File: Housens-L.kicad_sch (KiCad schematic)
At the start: 4 parts, among them U1 MCP1603

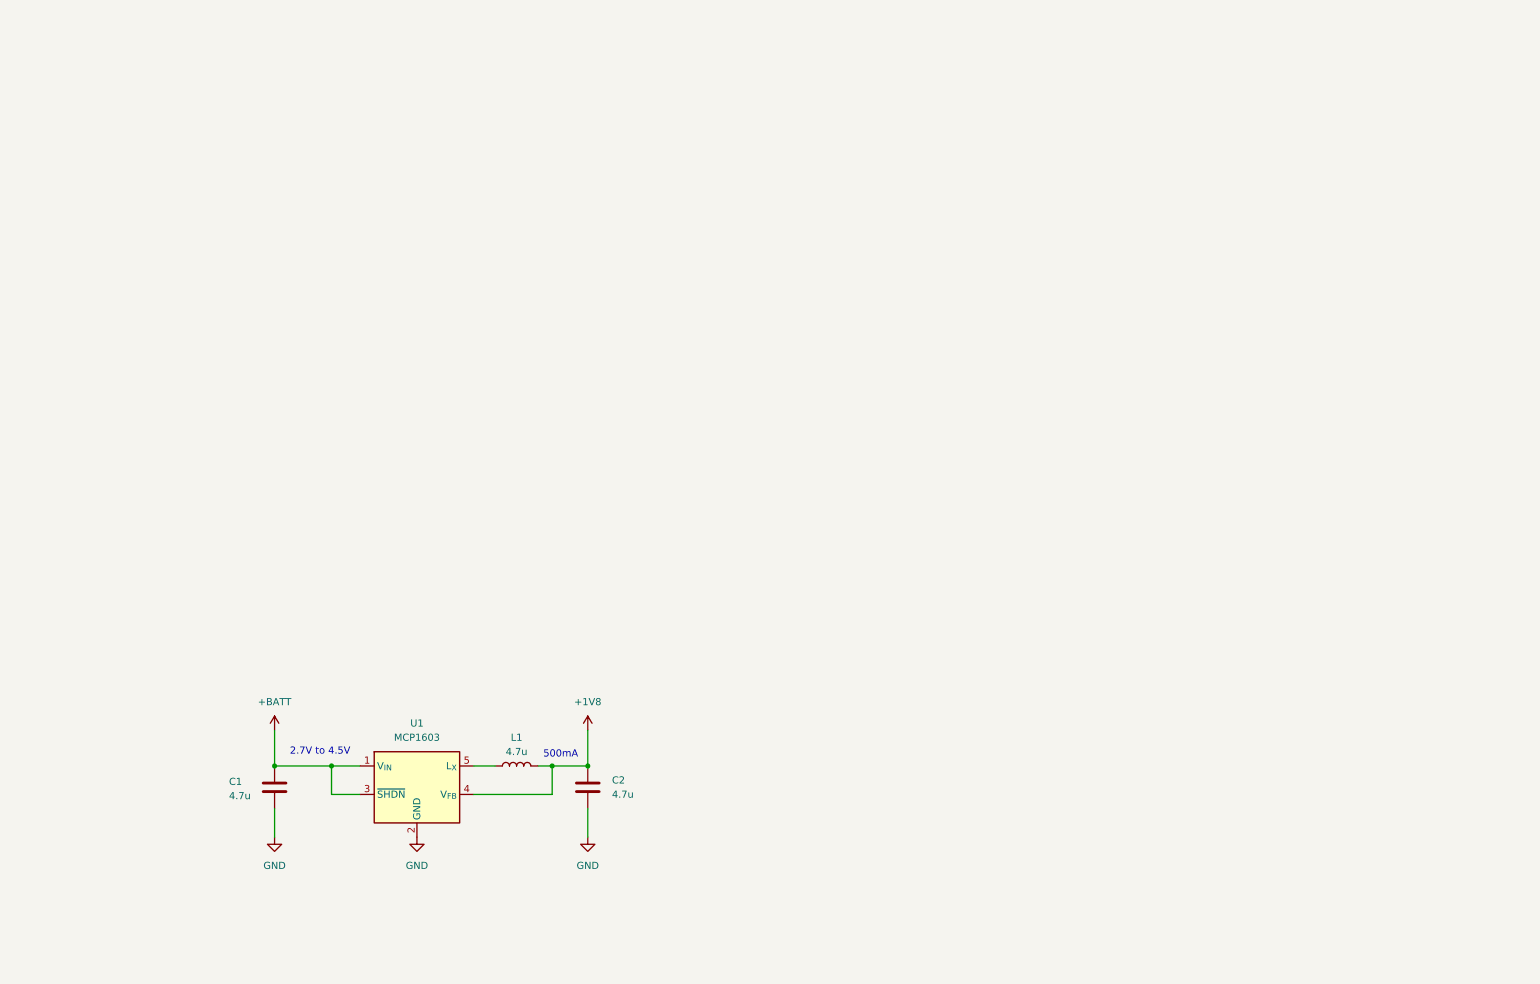
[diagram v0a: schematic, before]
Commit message: Add sensors
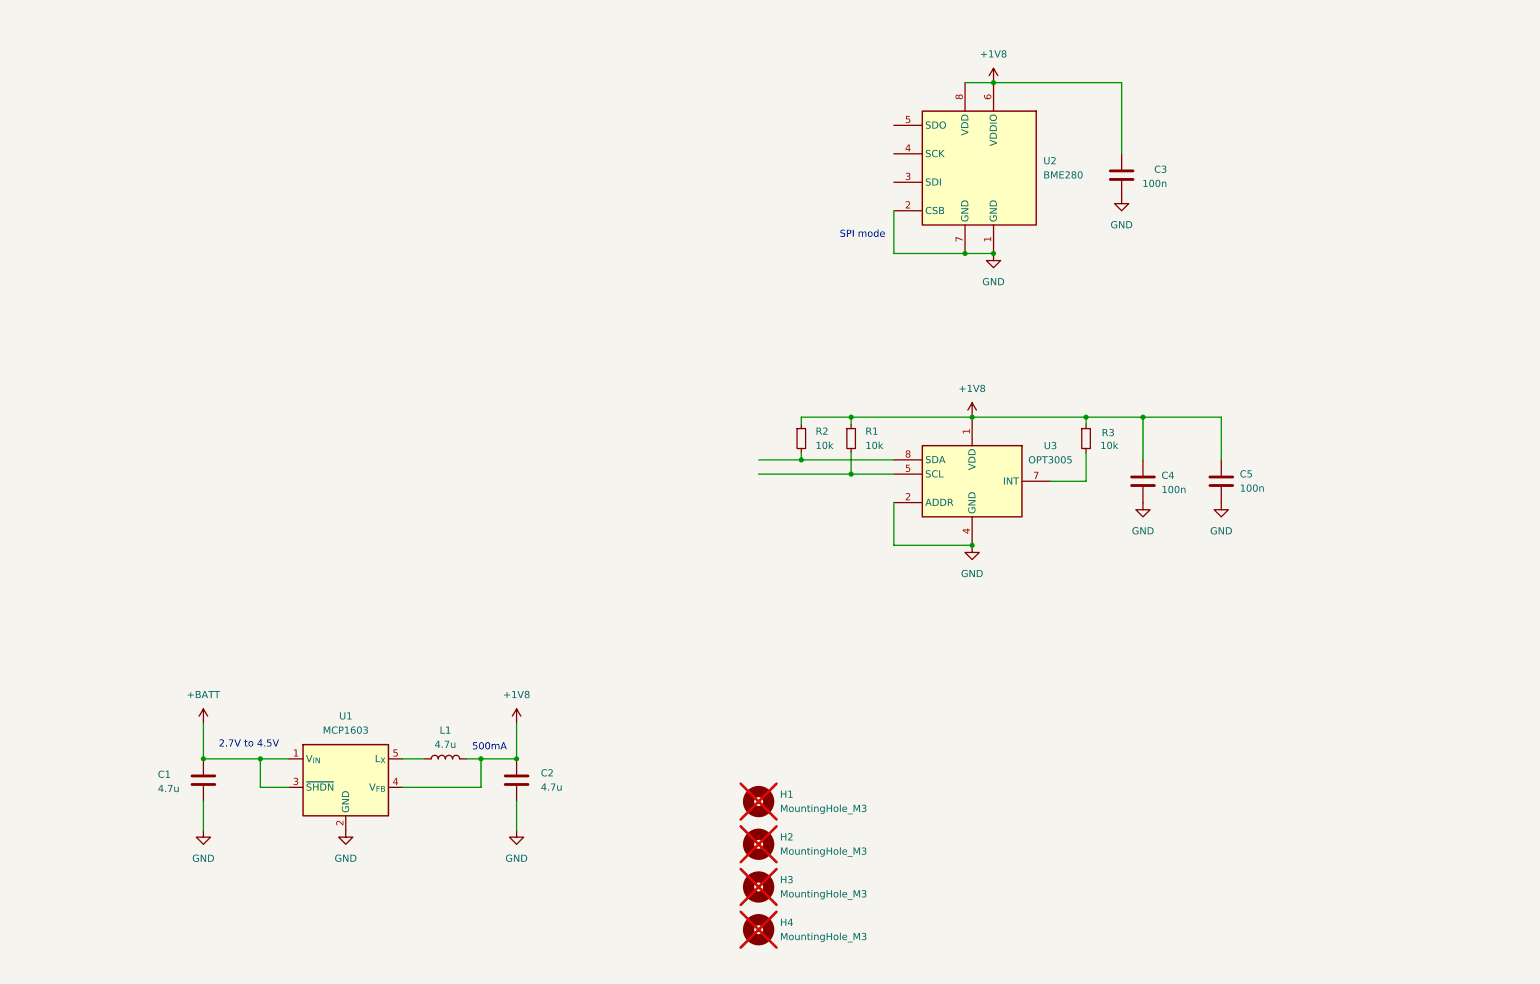
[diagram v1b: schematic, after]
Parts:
- added C3, C4, C5: 100n, Capacitor_SMD:C_0603_1608Metric, symbol Device:C
- added H1, H2, H3, H4: MountingHole_M3, MountingHole:MountingHole_3.2mm_M3, symbol PCM_SL_Mechanical:MountingHole_M3
- added R1, R2, R3: 10k, Resistor_SMD:R_0603_1608Metric, symbol Device:R_Small
- added U2: BME280, Package_LGA:Bosch_LGA-8_2.5x2.5mm_P0.65mm_ClockwisePinNumbering, symbol Sensor:BME280
- added U3: OPT3005, OPT3005DTSR, symbol PCM_OPT3005DTSR:OPT3005DTSR
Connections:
- net +1V8: now also C3.1, C4.1, C5.1, R1.1, R2.1, R3.1, U2.6 (VDDIO), U2.8 (VDD), U3.1 (VDD)
- net GND: now also C3.2, C4.2, C5.2, U2.1 (GND), U2.2 (CSB), U2.7 (GND), U3.2 (ADDR), U3.4 (GND)
- new net: R1.2, U3.5 (SCL)
- new net: R3.2, U3.7 (INT)
- new net: R2.2, U3.8 (SDA)
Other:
- note added: "SPI mode"
- moved on the sheet: C1, C2, L1, U1

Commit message: Add MCU
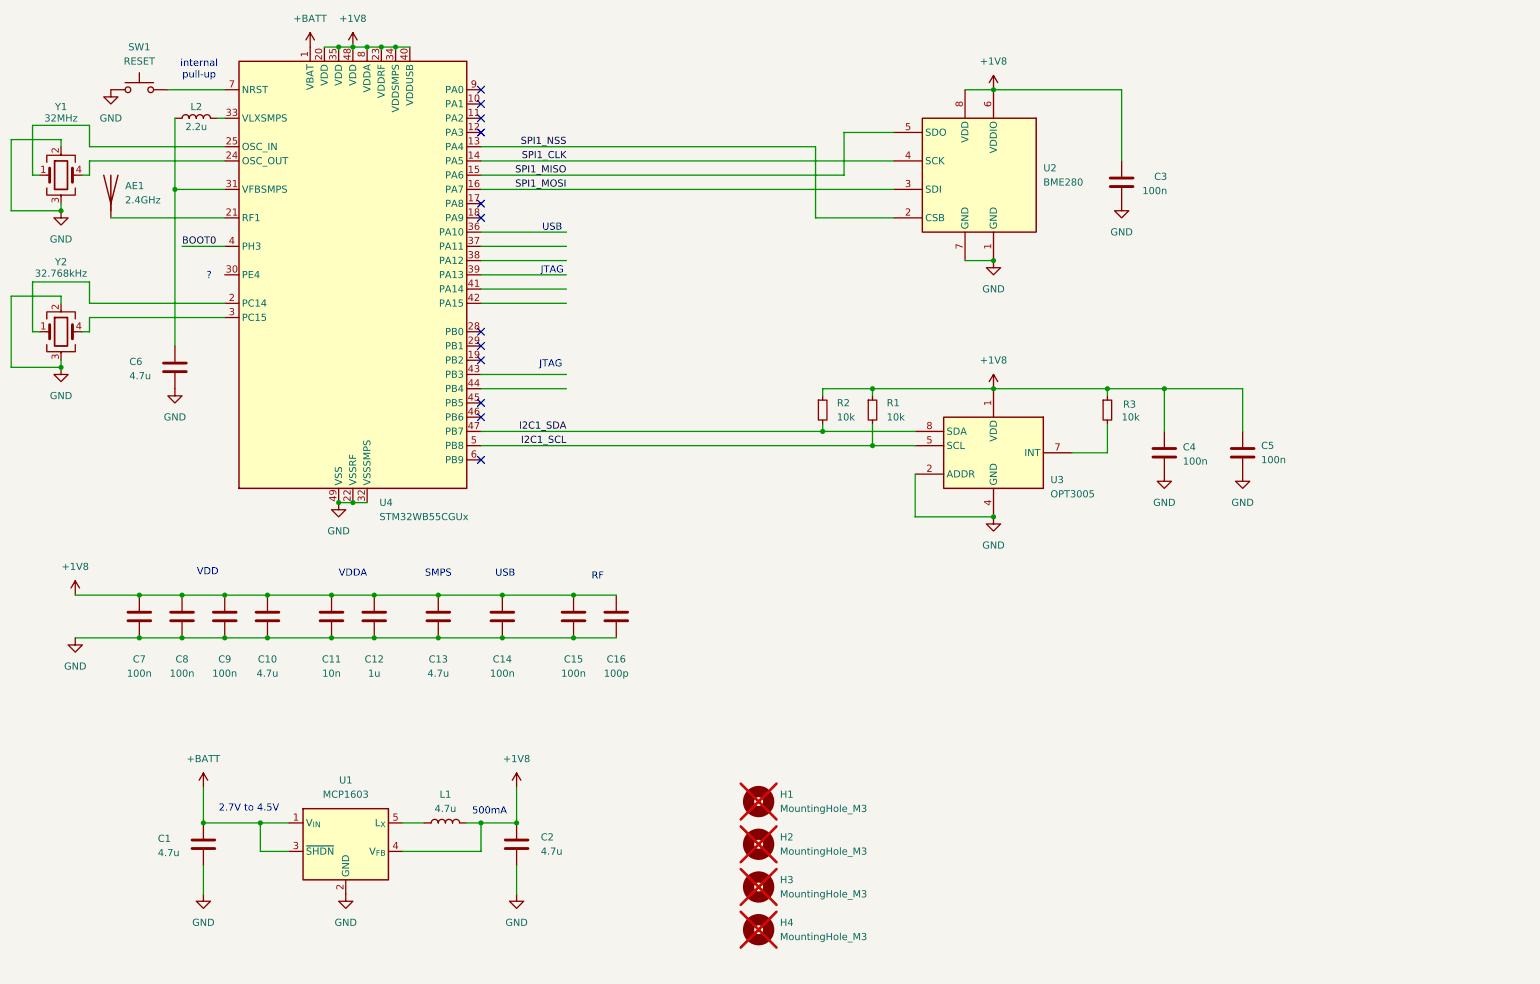
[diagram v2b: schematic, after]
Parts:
- added AE1: 2.4GHz, symbol Device:Antenna
- added C10, C13, C6: 4.7u, Capacitor_SMD:C_0603_1608Metric, symbol Device:C
- added C11: 10n, Capacitor_SMD:C_0603_1608Metric, symbol Device:C
- added C12: 1u, Capacitor_SMD:C_0603_1608Metric, symbol Device:C
- added C14, C15, C7, C8, C9: 100n, Capacitor_SMD:C_0603_1608Metric, symbol Device:C
- added C16: 100p, Capacitor_SMD:C_0603_1608Metric, symbol Device:C
- added L2: 2.2u, Inductor_SMD:L_Wuerth_WE-TPC-3816, symbol Device:L
- added SW1: RESET, Button_Switch_THT:SW_PUSH_6mm, symbol Switch:SW_Push
- added U4: STM32WB55CGUx, Package_DFN_QFN:QFN-48-1EP_7x7mm_P0.5mm_EP5.6x5.6mm, symbol MCU_ST_STM32WB:STM32WB55CGUx
- added Y1: 32MHz, symbol Device:Crystal_GND23
- added Y2: 32.768kHz, symbol Device:Crystal_GND23
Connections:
- net +1V8: now also C10.1, C11.1, C12.1, C13.1, C14.1, C15.1, C16.1, C7.1, C8.1, C9.1, U4.20 (VDD), U4.23 (VDDRF), U4.34 (VDDSMPS), U4.35 (VDD), U4.40 (VDDUSB), U4.48 (VDD), U4.8 (VDDA)
- net +BATT: now also U4.1 (VBAT)
- net GND: now also C10.2, C11.2, C12.2, C13.2, C14.2, C15.2, C16.2, C6.2, C7.2, C8.2, C9.2, SW1.1, U4.22 (VSSRF), U4.32 (VSSSMPS), U4.49 (VSS), Y1.2, Y1.3, Y2.2, Y2.3; no longer U2.2 (CSB)
- net I2C1_SCL: now reaches R1.2, U3.5 (SCL)
- net I2C1_SCL: now also U4.5 (PB8)
- net I2C1_SDA: now reaches R2.2, U3.8 (SDA)
- net I2C1_SDA: now also U4.47 (PB7)
- net SPI1_MOSI: now reaches U2.3 (SDI)
- net SPI1_MOSI: now also U4.16 (PA7)
- net SPI1_CLK: now reaches U2.4 (SCK)
- net SPI1_CLK: now also U4.14 (PA5)
- net SPI1_MISO: now reaches U2.5 (SDO)
- net SPI1_MISO: now also U4.15 (PA6)
- new net: U4.2 (PC14), Y2.1
- new net: AE1.1 (A), U4.21 (RF1)
- new net: U4.24 (OSC_OUT), Y1.4
- new net: U4.25 (OSC_IN), Y1.1
- new net: U4.3 (PC15), Y2.4
- new net: C6.1, L2.1, U4.31 (VFBSMPS)
- new net: L2.2, U4.33 (VLXSMPS)
- new net: SW1.2, U4.7 (NRST)
- new net BOOT0: U4.4 (PH3)
- new net SPI1_NSS: U2.2 (CSB), U4.13 (PA4)
- no-connect marks 0 -> 12
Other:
- note added: "?"
- note added: "JTAG"
- note added: "RF"
- note added: "SMPS"
- note added: "USB"
- note added: "VDD"
- note added: "VDDA"
- note added: "internal pull-up"
- note removed: "SPI mode"
- moved on the sheet: C1, C2, C3, C4, C5, L1, R1, R2, R3, U1, U2, U3

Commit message: Add battery
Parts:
- added BT1: CR2032, Battery:BatteryHolder_Keystone_3002_1x2032, symbol Device:Battery_Cell
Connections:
- net +BATT: now also BT1.1 (+)
- net GND: now also BT1.2 (-)
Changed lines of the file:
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@@
 	)
 	(junction
+		(at 49.53 177.8)
+		(diameter 0)
+		(color 0 0 0 0)
+	)
+	(junction
 		(at 190.5 39.37)
 		(diameter 0)
@@
 	(wire
 		(pts
+			(xy 30.48 170.18) (xy 49.53 170.18)
+		)
+		(stroke
+			(width 0)
+			(type default)
+		)
+	)
+	(wire
+		(pts
 			(xy 99.06 49.53) (xy 158.75 49.53)
 		)
@@
 	(wire
 		(pts
+			(xy 30.48 177.8) (xy 49.53 177.8)
+		)
+		(stroke
+			(width 0)
+			(type default)
+		)
+	)
+	(wire
+		(pts
 			(xy 99.06 175.26) (xy 99.06 170.18)
 		)
@@
 					(unit 1)
 				)
+			)
+		)
+	)
+	(symbol
+		(lib_id "Device:Battery_Cell")
+		(at 30.48 175.26 0)
+		(unit 1)
+		(exclude_from_sim no)
+		(in_bom yes)
+		(on_board yes)
+		(dnp no)
+		(property "Reference" "BT1"
+			(at 26.67 172.1484 0)
+			(effects
+				(font
+					(size 1.27 1.27)
+				)
+				(justify right)
+			)
+		)
+		(property "Value" "CR2032"
+			(at 26.67 174.6884 0)
+			(effects
+				(font
+					(size 1.27 1.27)
+				)
+				(justify right)
+			)
+		)
+		(property "Footprint" "Battery:BatteryHolder_Keystone_3002_1x2032"
+			(at 30.48 173.736 90)
+			(effects
+				(font
+					(size 1.27 1.27)
+				)
+				(hide yes)
+			)
+		)
+		(property "Datasheet" "~"
+			(at 30.48 173.736 90)
+			(effects
+				(font
+					(size 1.27 1.27)
+				)
+				(hide yes)
+			)
+		)
+		(property "Description" "Single-cell battery"
+			(at 30.48 175.26 0)
+			(effects
+				(font
+					(size 1.27 1.27)
+				)
+				(hide yes)
+			)
+		)
+		(pin "1"
+		)
+		(pin "2"
+		)
+		(instances
+			(project ""
+				(path "/36bb4837-104c-4aa4-b300-0e6d0ff24db5"
+					(reference "BT1")
+					(unit 1)
+				)

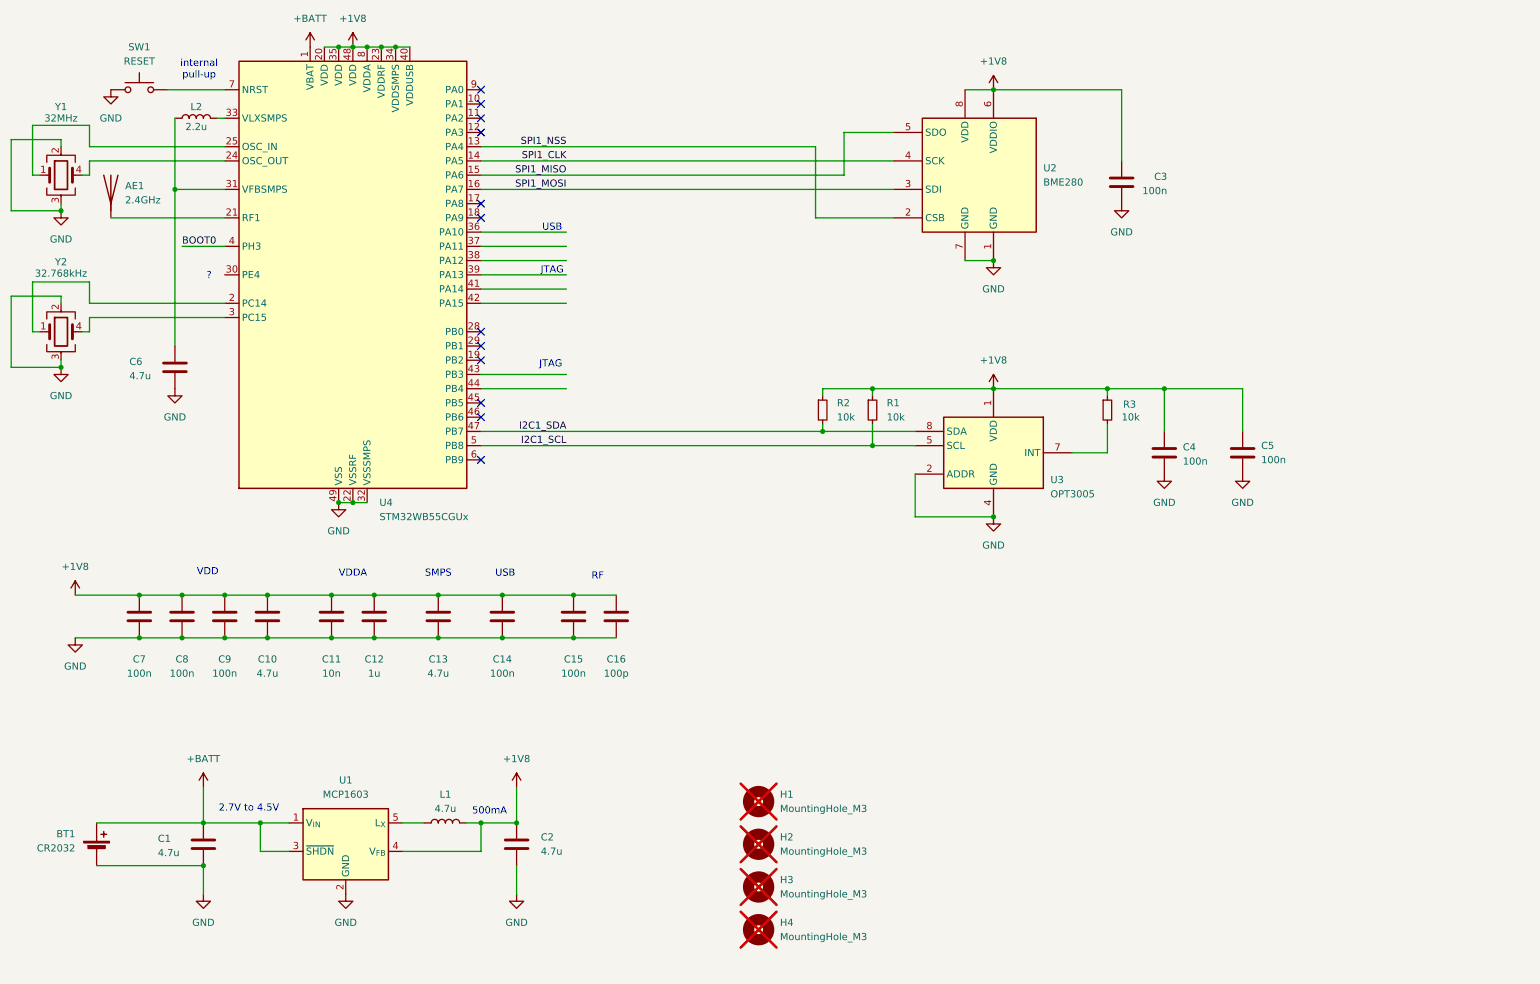
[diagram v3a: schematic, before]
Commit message: Add debug connector
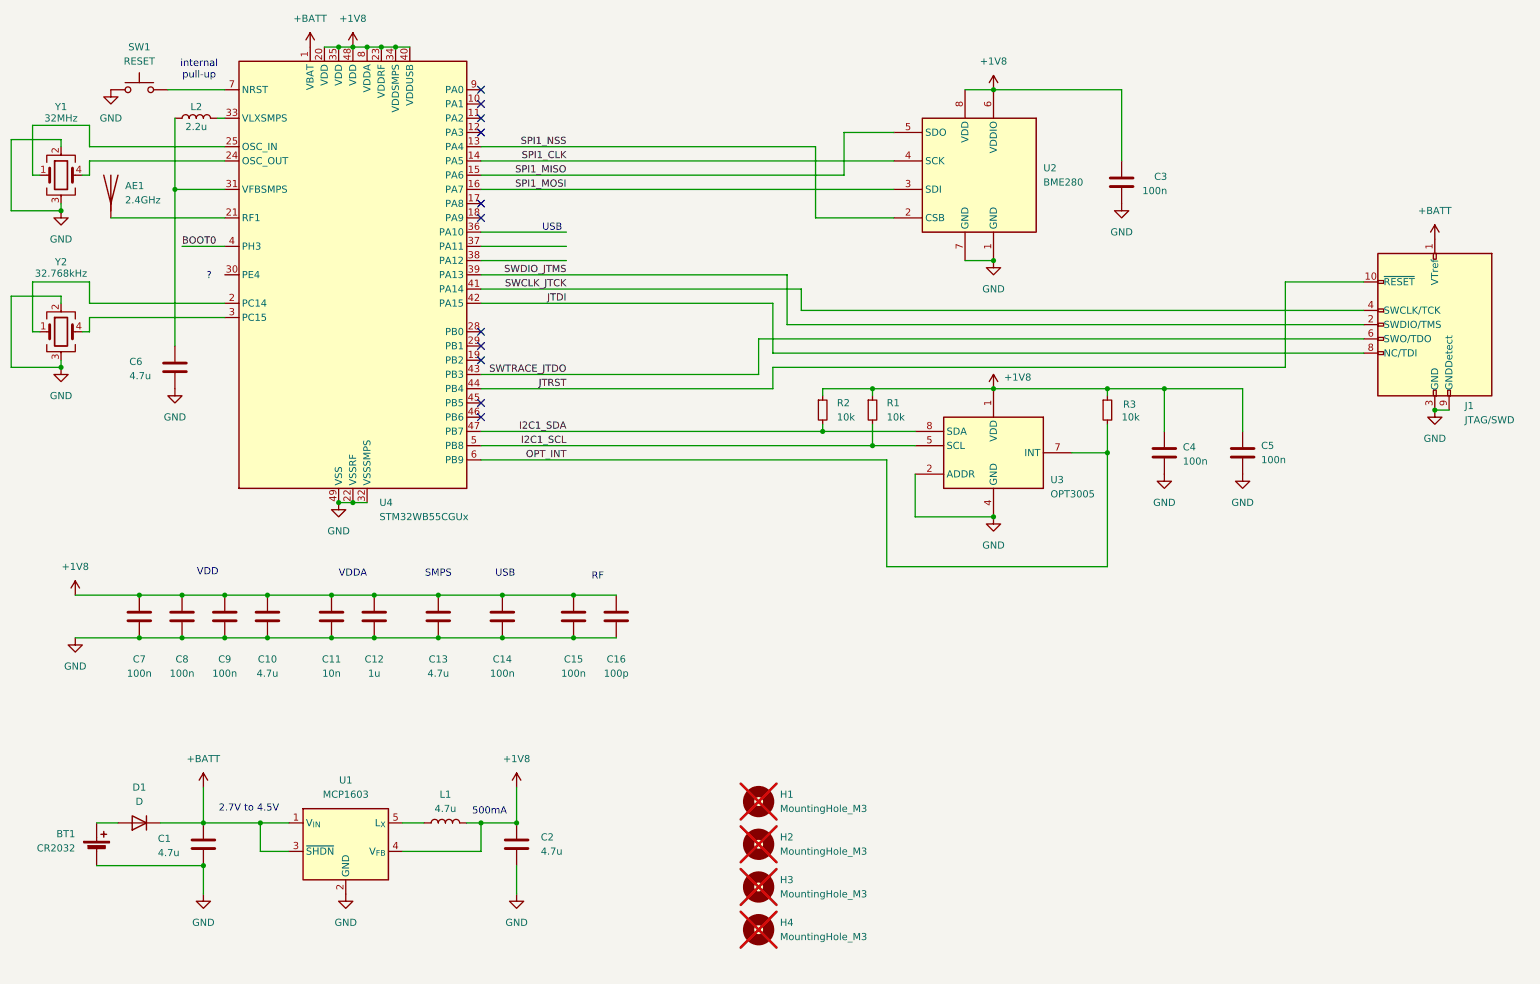
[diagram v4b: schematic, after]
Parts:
- added D1: D, Diode_SMD:D_0603_1608Metric, symbol Device:D
- added J1: JTAG/SWD, Connector_PinHeader_1.27mm:PinHeader_2x05_P1.27mm_Vertical_SMD, symbol Connector:Conn_ARM_JTAG_SWD_10
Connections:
- net +BATT: now also D1.1 (K), J1.1 (VTref); no longer BT1.1 (+)
- net GND: now also J1.3 (GND), J1.5 (GND), J1.9 (GNDDetect)
- net SWDIO_JTMS: now reaches U4.39 (PA13)
- net SWDIO_JTMS: now also J1.2 (SWDIO/TMS)
- net SWCLK_JTCK: now reaches U4.41 (PA14)
- net SWCLK_JTCK: now also J1.4 (SWCLK/TCK)
- net JTDI: now reaches U4.42 (PA15)
- net JTDI: now also J1.8 (NC/TDI)
- net SWTRACE_JTDO: now reaches U4.43 (PB3)
- net SWTRACE_JTDO: now also J1.6 (SWO/TDO)
- net JTRST: now reaches U4.44 (PB4)
- net JTRST: now also J1.10 (~{RESET})
- net OPT_INT: now reaches U4.6 (PB9)
- net OPT_INT: now also R3.2, U3.7 (INT)
- new net: BT1.1 (+), D1.2 (A)
- no-connect marks 12 -> 11
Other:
- note removed: "JTAG"
